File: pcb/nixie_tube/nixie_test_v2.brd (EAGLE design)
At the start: 25.4 x 41.9 mm, 8 parts

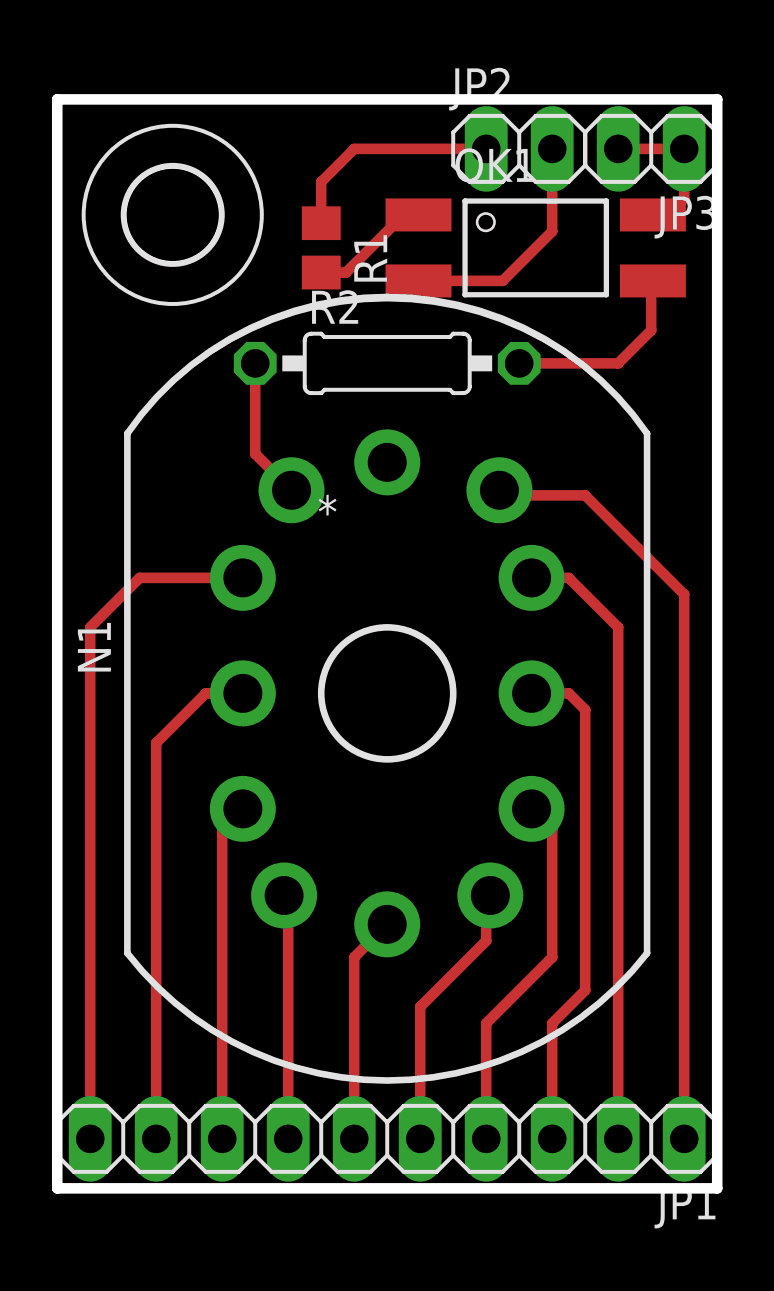
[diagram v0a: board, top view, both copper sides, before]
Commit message: 
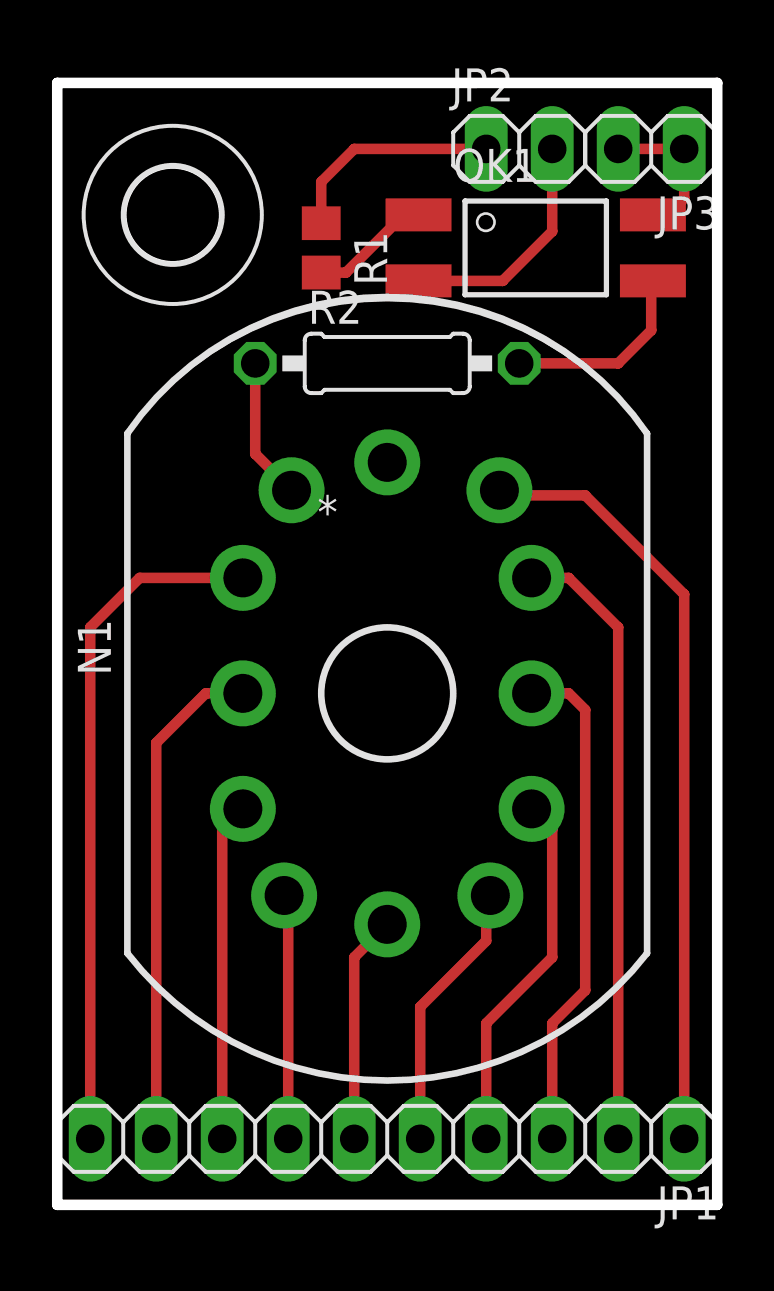
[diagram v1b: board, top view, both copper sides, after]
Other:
- board size 25.4 x 41.9 mm -> 25.4 x 43.2 mm
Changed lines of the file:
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@@
 <board>
 <plain>
-<wire x1="0" y1="0" x2="25.4" y2="0" width="0.4064" layer="20"/>
-<wire x1="25.4" y1="0" x2="25.4" y2="41.91" width="0.4064" layer="20"/>
-<wire x1="25.4" y1="41.91" x2="0" y2="41.91" width="0.4064" layer="20"/>
-<wire x1="0" y1="41.91" x2="0" y2="0" width="0.4064" layer="20"/>
+<wire x1="0" y1="-0.635" x2="25.4" y2="-0.635" width="0.4064" layer="20"/>
+<wire x1="25.4" y1="-0.635" x2="25.4" y2="42.545" width="0.4064" layer="20"/>
+<wire x1="25.4" y1="42.545" x2="0" y2="42.545" width="0.4064" layer="20"/>
+<wire x1="0" y1="42.545" x2="0" y2="-0.635" width="0.4064" layer="20"/>
 </plain>
 <attributes>
